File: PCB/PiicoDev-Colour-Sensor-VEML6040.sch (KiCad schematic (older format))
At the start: 22 parts, among them J1 , J2 , J3 Conn_PiicoDev_header_01x04_Ma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, J4 Conn_01x01_Male, Q1 BSS138, U1 VEML6040

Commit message: Add LED current note
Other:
- note added: "68 Ohms draws 8.4 mA"
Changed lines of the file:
@@
 Text Label 4300 6600 0    50   ~ 0
 LED_EN
+Text Notes 2450 3800 0    50   ~ 0
+68 Ohms draws 8.4 mA
 $EndSCHEMATC

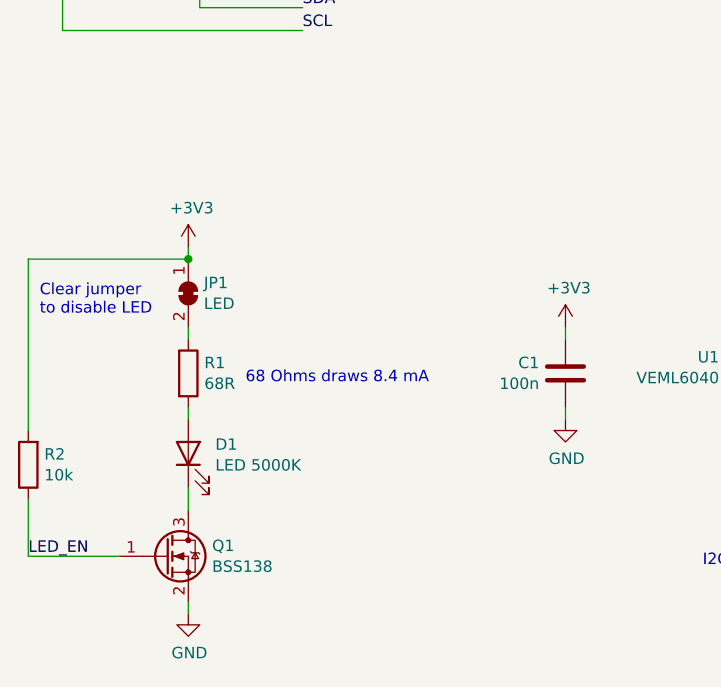
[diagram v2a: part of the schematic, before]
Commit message: Add LED bypass resistor
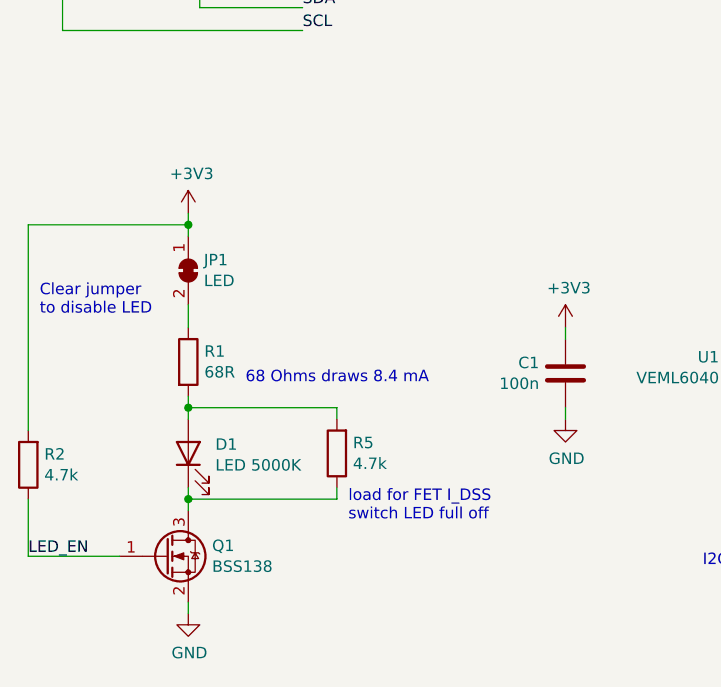
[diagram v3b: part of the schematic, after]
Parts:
- added R5: 4.7k, Resistor_SMD:R_0402_1005Metric, symbol Device:R
- R2: value 10k -> 4.7k
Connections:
- net at D1.1 (K), Q1.3 (D): now also R5.1
- net at D1.2 (A), R1.2: now also R5.2
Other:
- note added: "load for FET I_DSS\nswitch LED full off"
- moved on the sheet: JP1, R1
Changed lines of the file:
@@
 L power:+3V3 #PWR0106
 U 1 1 5F914ABC
-P 2200 3200
-F 0 "#PWR0106" H 2200 3050 50  0001 C CNN
-F 1 "+3V3" H 2215 3373 50  0000 C CNN
-F 2 "" H 2200 3200 50  0001 C CNN
-F 3 "" H 2200 3200 50  0001 C CNN
-	1    2200 3200
+P 2200 3050
+F 0 "#PWR0106" H 2200 2900 50  0001 C CNN
+F 1 "+3V3" H 2215 3223 50  0000 C CNN
+F 2 "" H 2200 3050 50  0001 C CNN
+F 3 "" H 2200 3050 50  0001 C CNN
+	1    2200 3050
 	1    0    0    -1
 $EndComp
@@
 L Jumper:SolderJumper_2_Bridged JP1
 U 1 1 5F9150B4
-P 2200 3400
-F 0 "JP1" V 2154 3468 50  0000 L CNN
-F 1 "LED" V 2245 3468 50  0000 L CNN
-F 2 "Jumper:SolderJumper-2_P1.3mm_Bridged_RoundedPad1.0x1.5mm" H 2200 3400 50  0001 C CNN
-F 3 "~" H 2200 3400 50  0001 C CNN
-	1    2200 3400
+P 2200 3300
+F 0 "JP1" V 2154 3368 50  0000 L CNN
+F 1 "LED" V 2245 3368 50  0000 L CNN
+F 2 "Jumper:SolderJumper-2_P1.3mm_Bridged_RoundedPad1.0x1.5mm" H 2200 3300 50  0001 C CNN
+F 3 "~" H 2200 3300 50  0001 C CNN
+	1    2200 3300
 	0    1    1    0
 $EndComp
-Wire Wire Line
-	2200 3250 2200 3200
 $Comp
 L Device:R R1
 U 1 1 5F915BCC
-P 2200 3750
-F 0 "R1" H 2270 3796 50  0000 L CNN
-F 1 "68R" H 2270 3705 50  0000 L CNN
-F 2 "Resistor_SMD:R_0402_1005Metric" V 2130 3750 50  0001 C CNN
-F 3 "~" H 2200 3750 50  0001 C CNN
-	1    2200 3750
-	1    0    0    -1
-$EndComp
-Wire Wire Line
-	2200 3600 2200 3550
+P 2200 3700
+F 0 "R1" H 2270 3746 50  0000 L CNN
+F 1 "68R" H 2270 3655 50  0000 L CNN
+F 2 "Resistor_SMD:R_0402_1005Metric" V 2130 3700 50  0001 C CNN
+F 3 "~" H 2200 3700 50  0001 C CNN
+	1    2200 3700
+	1    0    0    -1
+$EndComp
 Wire Wire Line
 	2200 3950 2200 3900
@@
 $EndComp
 Wire Wire Line
-	2200 4250 2200 4350
+	2200 4250 2200 4300
 Wire Wire Line
 	2200 4750 2200 4800
@@
 	1    0    0    -1
 $EndComp
-Connection ~ 2200 3250
 Text Notes 1550 3500 0    50   ~ 0
 Clear jumper \nto disable LED
@@
 P 1500 4150
 F 0 "R2" H 1430 4104 50  0000 R CNN
-F 1 "10k" H 1430 4195 50  0000 R CNN
+F 1 "4.7k" H 1430 4195 50  0000 R CNN
 F 2 "Resistor_SMD:R_0402_1005Metric" V 1430 4150 50  0001 C CNN
 F 3 "~" H 1500 4150 50  0001 C CNN
@@
 Wire Wire Line
 	1500 4550 1500 4300
-Wire Wire Line
-	1500 4000 1500 3250
-Wire Wire Line
-	1500 3250 2200 3250
 Text Label 1500 4550 0    50   ~ 0
 LED_EN
@@
 Text Notes 2450 3800 0    50   ~ 0
 68 Ohms draws 8.4 mA
+$Comp
+L Device:R R5
+U 1 1 6124B54E
+P 2850 4100
+F 0 "R5" H 2780 4054 50  0000 R CNN
+F 1 "4.7k" H 2780 4145 50  0000 R CNN
+F 2 "Resistor_SMD:R_0402_1005Metric" V 2780 4100 50  0001 C CNN
+F 3 "~" H 2850 4100 50  0001 C CNN
+	1    2850 4100
+	-1   0    0    1
+$EndComp
+Wire Wire Line
+	2200 4300 2850 4300
+Wire Wire Line
+	2850 4300 2850 4250
+Connection ~ 2200 4300
+Wire Wire Line
+	2200 4300 2200 4350
+Wire Wire Line
+	2850 3950 2850 3900
+Wire Wire Line
+	2850 3900 2200 3900
+Connection ~ 2200 3900
+Wire Wire Line
+	2200 3850 2200 3900
+Wire Wire Line
+	2200 3550 2200 3450
+Wire Wire Line
+	2200 3050 2200 3100
+Wire Wire Line
+	2200 3100 1500 3100
+Wire Wire Line
+	1500 3100 1500 4000
+Connection ~ 2200 3100
+Wire Wire Line
+	2200 3100 2200 3150
+Text Notes 2900 4400 0    50   ~ 0
+load for FET I_DSS\nswitch LED full off
 $EndSCHEMATC
